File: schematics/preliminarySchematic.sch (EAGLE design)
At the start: 37 parts, among them IC1 74LS47N, IC2 74LS138N, Q1 2N3906, Q2 2N3906, U1 328P

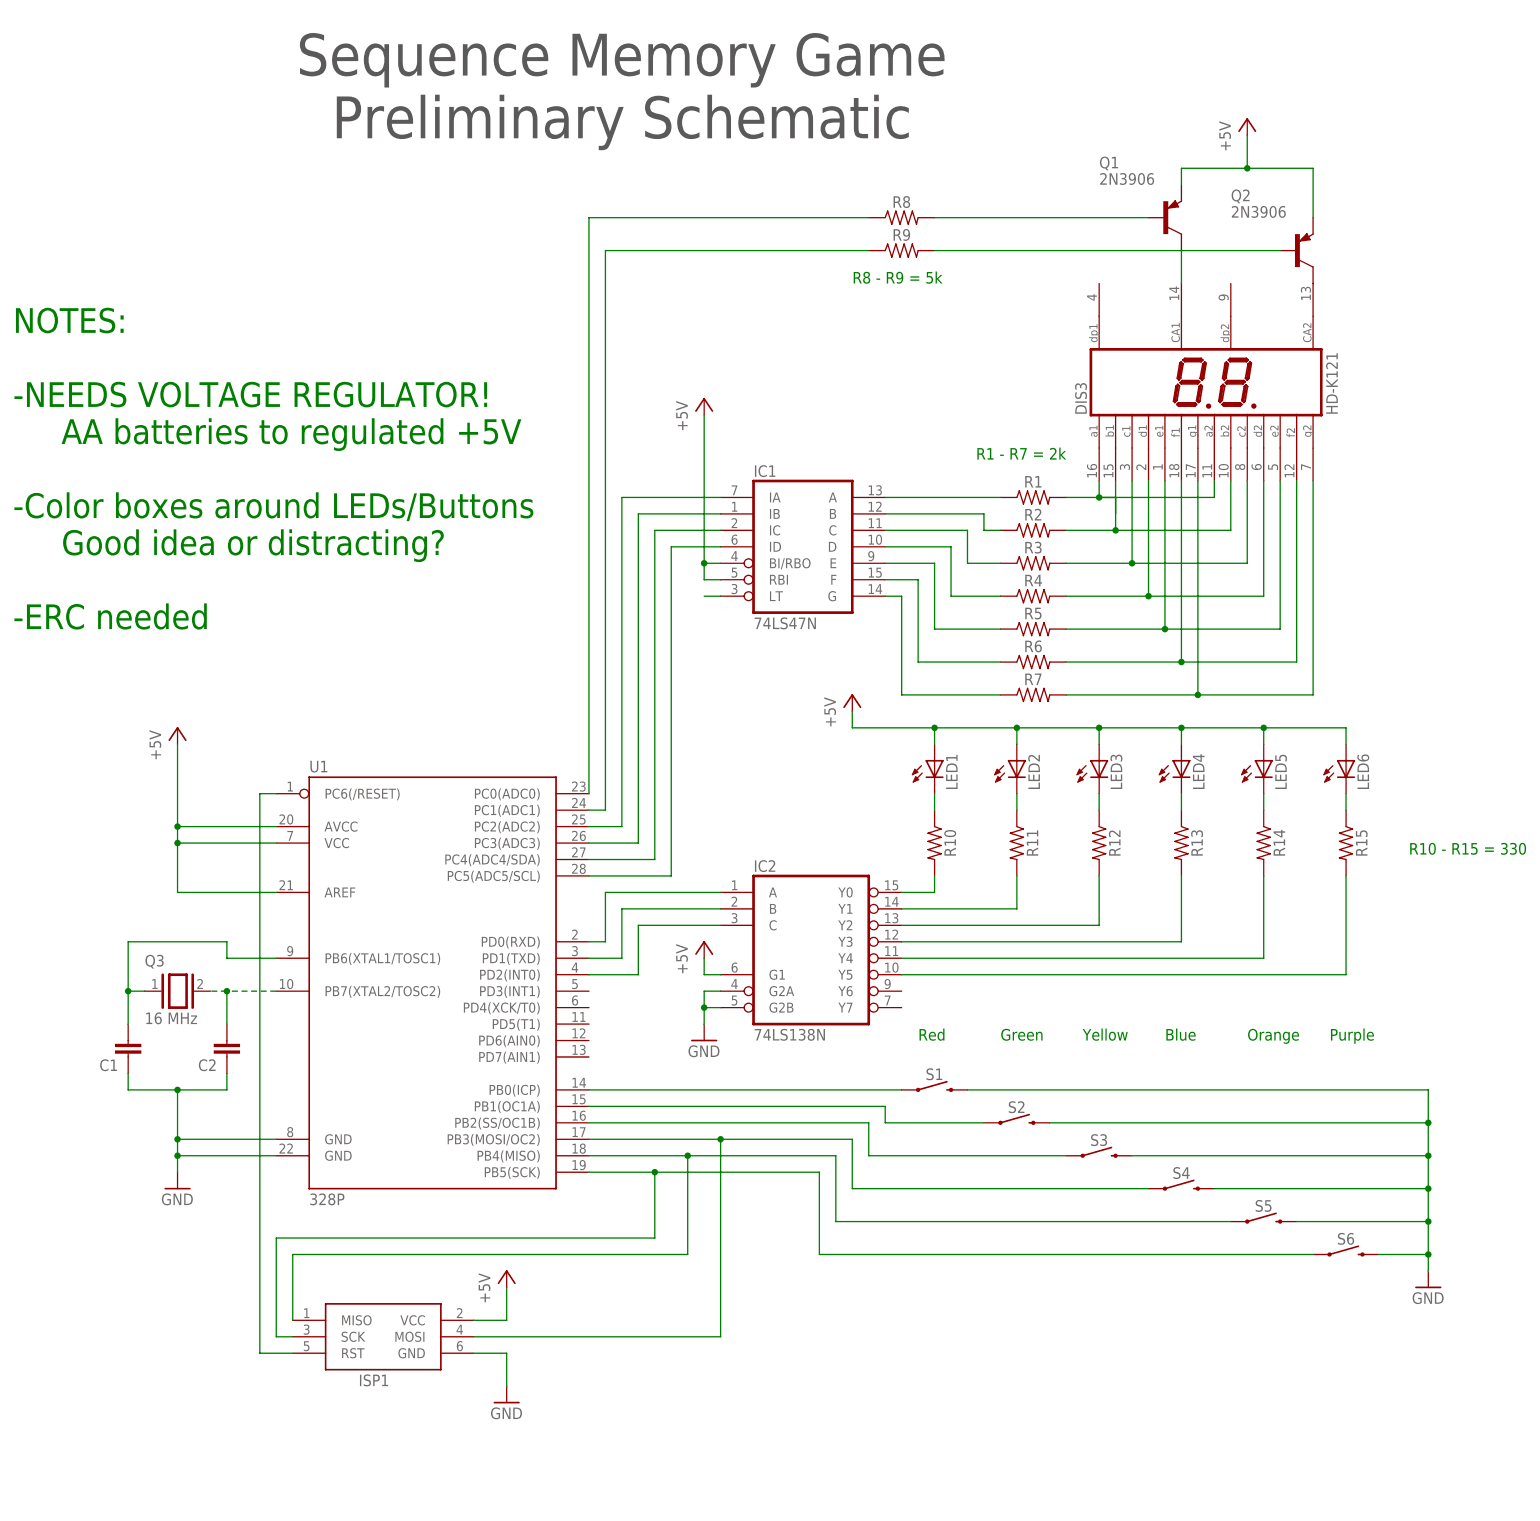
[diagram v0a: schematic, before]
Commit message: added audio amp and speaker
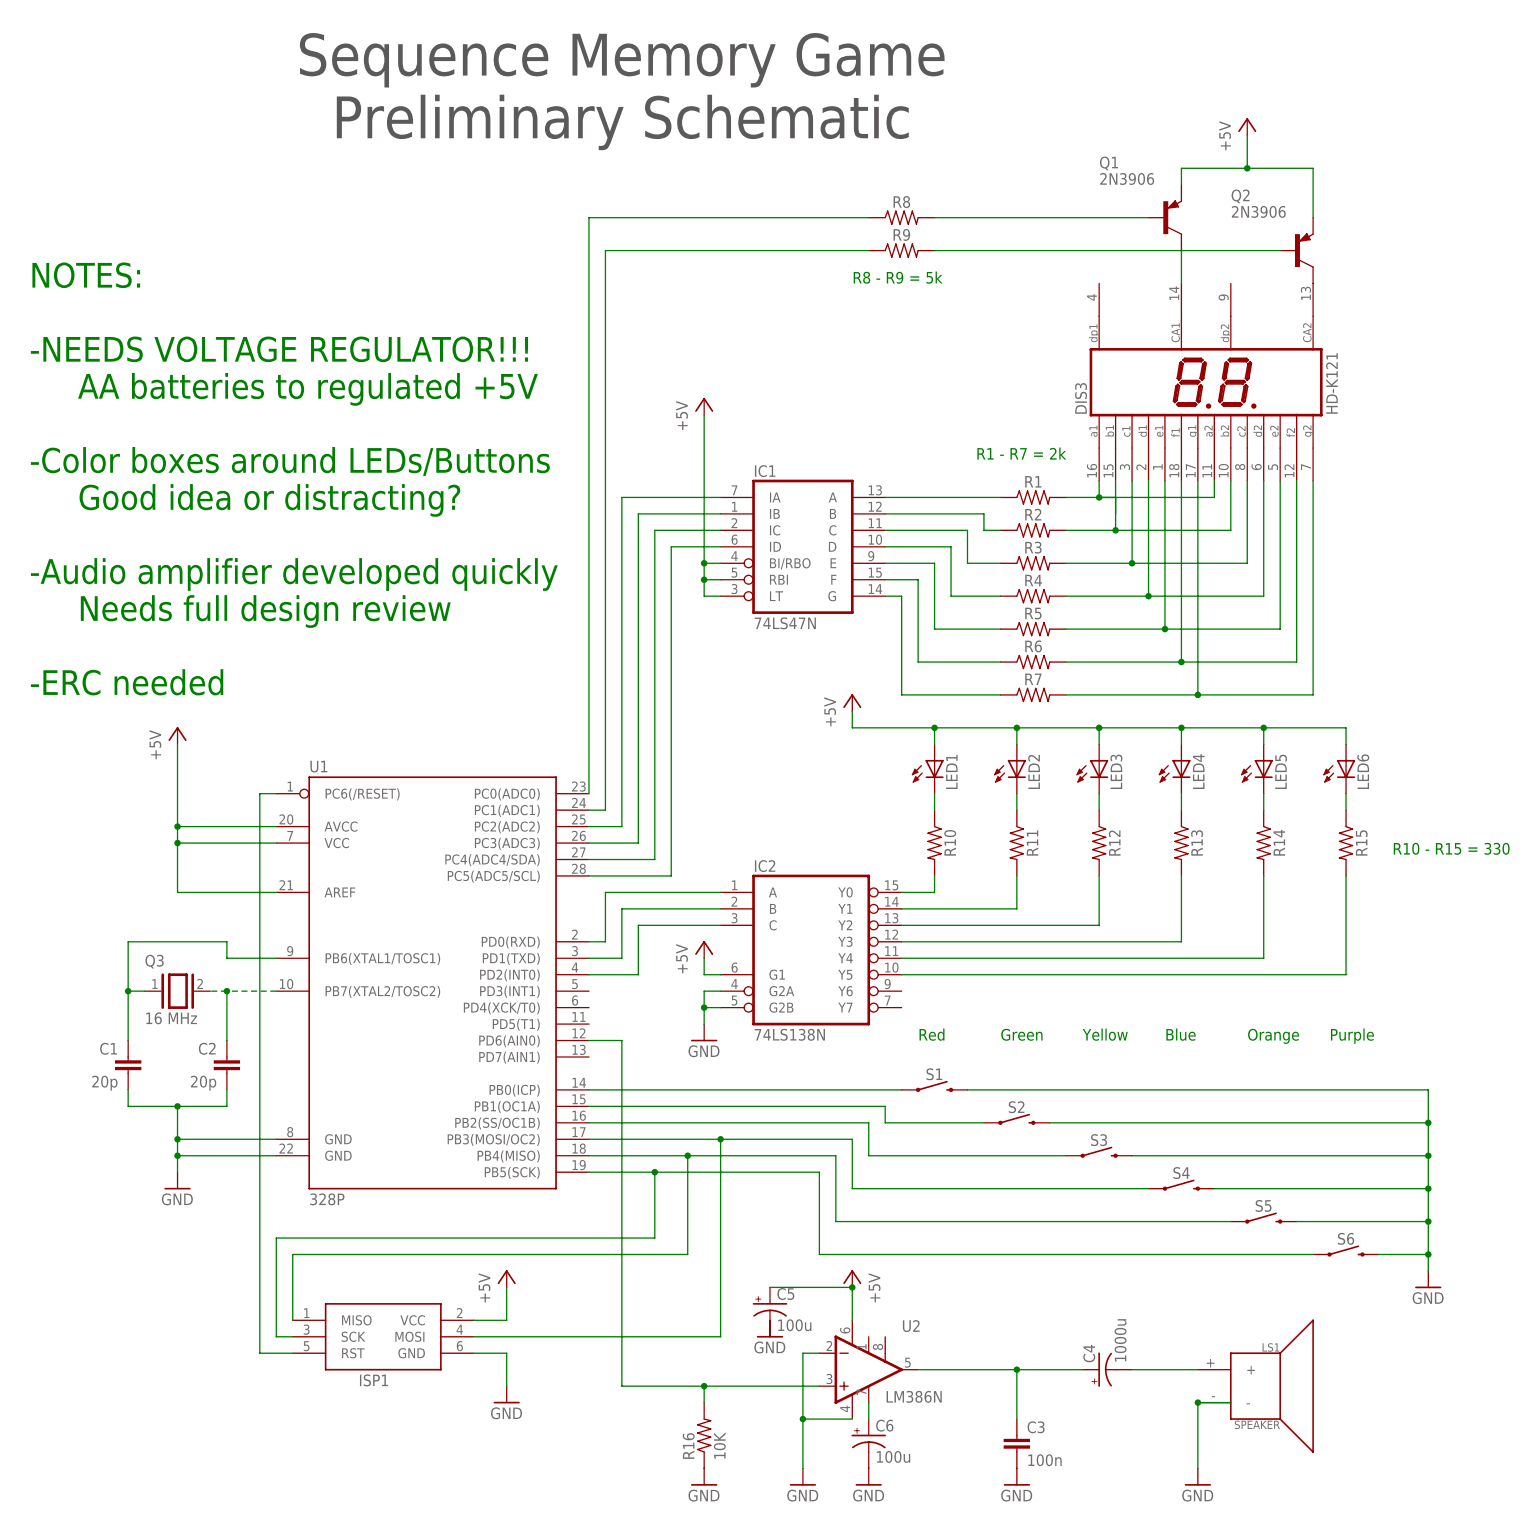
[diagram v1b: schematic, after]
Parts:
- added C3: 100n, capacitor-wima:C2,5-3
- added C4: 1000u, rcl:CPOL-USE5-10.5
- added C5, C6: 100u, rcl:CPOL-USE2.5-6
- added LS1: SPEAKER, SparkFun-Electromechanical:SPEAKER
- added R16: 10K, rcl:R-US_0204/5
- added U2: LM386N, SparkFun-IC-Amplifiers:LM386
- C1, C2: value (none) -> 20p
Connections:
- removed net N$30: IC1G$1.LT
- new net N$32: R16.2, U1.PD6(AIN0), U2.+IN
- new net N$40: C6.+, U2.BP
- new net N$46: C3.1, C4.+, U2.OUT
- new net N$50: C4.-, LS1.+
- net +5V: now also C5.+, IC1G$1.LT, U2.V+
- net GND: now also C1.2, C2.2, C3.2, C6.-, LS1.-, R16.1, U2.-IN, U2.V-; no longer C1.1, C2.1
- net N$16: now also C2.1; no longer C2.2
- net N$23: now also C1.1; no longer C1.2
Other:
- note added: "NOTES: -NEEDS VOLTAGE REGULATOR!!! AA batteries to regulated +5V -Color boxes around LEDs/Buttons Good idea or distracting? -Audio amplifier developed quickly Needs full design review -ERC needed"
- note removed: "NOTES: -NEEDS VOLTAGE REGULATOR! AA batteries to regulated +5V -Color boxes around LEDs/Buttons Good idea or distracting? -ERC needed"
- moved on the sheet: C1, C2
